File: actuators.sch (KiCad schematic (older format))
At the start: 16 parts

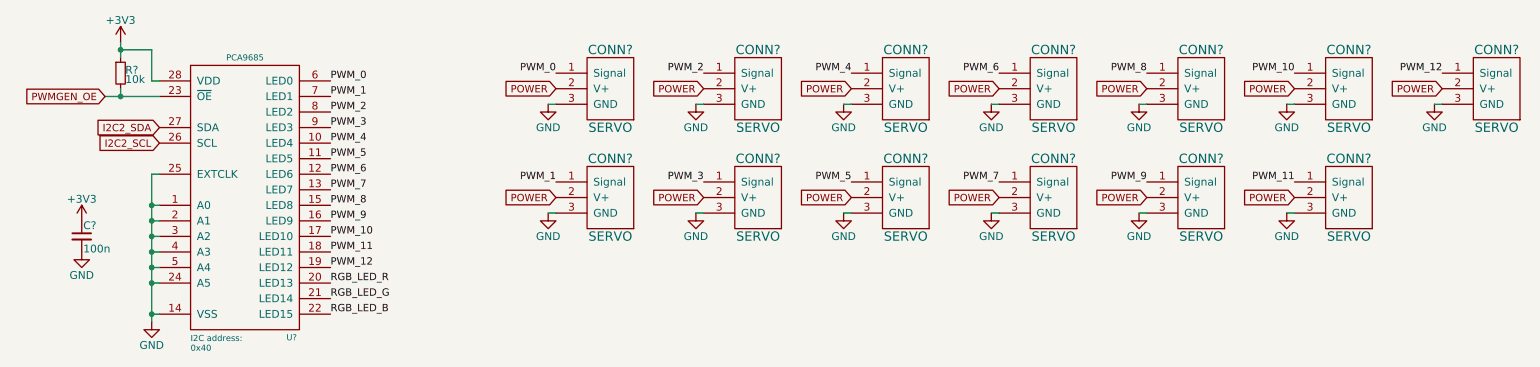
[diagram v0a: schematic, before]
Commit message: Add power from CAN bus and switch to hierarchical labelling
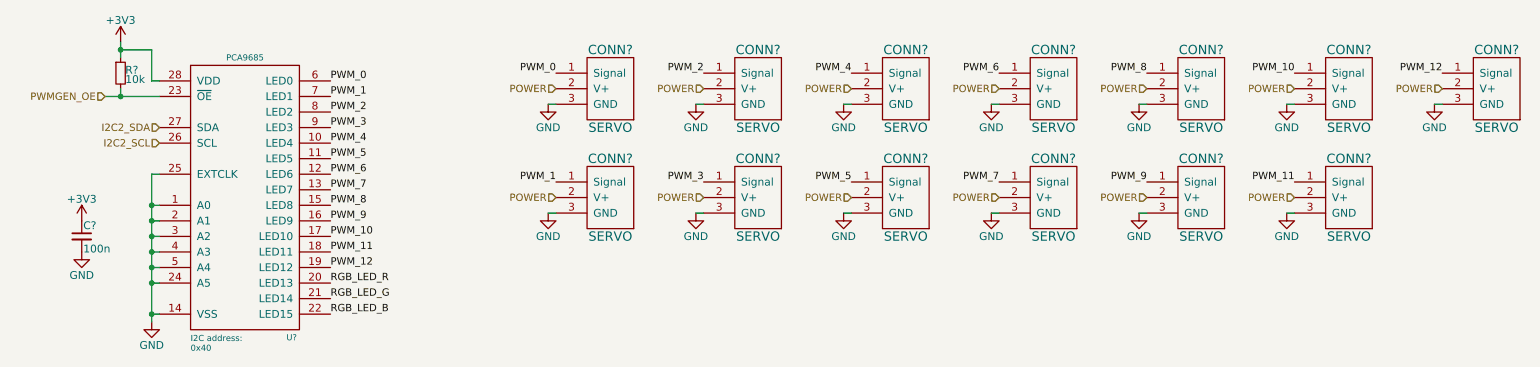
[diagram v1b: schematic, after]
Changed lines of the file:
@@
 Text Label 4300 1250 2    47   ~ 0
 PWM_0
-Text GLabel 4300 1350 0    47   Input ~ 0
-POWER
 $Comp
 L GND #PWR?
@@
 Text Label 5250 1250 2    47   ~ 0
 PWM_2
-Text GLabel 5250 1350 0    47   Input ~ 0
-POWER
 $Comp
 L GND #PWR?
@@
 Text Label 4300 1950 2    47   ~ 0
 PWM_1
-Text GLabel 4300 2050 0    47   Input ~ 0
-POWER
 $Comp
 L GND #PWR?
@@
 Text Label 5250 1950 2    47   ~ 0
 PWM_3
-Text GLabel 5250 2050 0    47   Input ~ 0
-POWER
 $Comp
 L GND #PWR?
@@
 Text Label 6200 1250 2    47   ~ 0
 PWM_4
-Text GLabel 6200 1350 0    47   Input ~ 0
-POWER
 $Comp
 L GND #PWR?
@@
 Text Label 7150 1250 2    47   ~ 0
 PWM_6
-Text GLabel 7150 1350 0    47   Input ~ 0
-POWER
 $Comp
 L GND #PWR?
@@
 Text Label 6200 1950 2    47   ~ 0
 PWM_5
-Text GLabel 6200 2050 0    47   Input ~ 0
-POWER
 $Comp
 L GND #PWR?
@@
 Text Label 7150 1950 2    47   ~ 0
 PWM_7
-Text GLabel 7150 2050 0    47   Input ~ 0
-POWER
 $Comp
 L GND #PWR?
@@
 Text Label 8100 1250 2    47   ~ 0
 PWM_8
-Text GLabel 8100 1350 0    47   Input ~ 0
-POWER
 $Comp
 L GND #PWR?
@@
 Text Label 9050 1250 2    47   ~ 0
 PWM_10
-Text GLabel 9050 1350 0    47   Input ~ 0
-POWER
 $Comp
 L GND #PWR?
@@
 Text Label 8100 1950 2    47   ~ 0
 PWM_9
-Text GLabel 8100 2050 0    47   Input ~ 0
-POWER
 $Comp
 L GND #PWR?
@@
 Text Label 9050 1950 2    47   ~ 0
 PWM_11
-Text GLabel 9050 2050 0    47   Input ~ 0
-POWER
 $Comp
 L GND #PWR?
@@
 Text Label 10000 1250 2    47   ~ 0
 PWM_12
-Text GLabel 10000 1350 0    47   Input ~ 0
-POWER
 $Comp
 L GND #PWR?
@@
 Wire Wire Line
 	9950 1450 10000 1450
-Text GLabel 1750 1600 0    47   Input ~ 0
+Text HLabel 1750 1600 0    47   Input ~ 0
 I2C2_SDA
-Text GLabel 1750 1700 0    47   Input ~ 0
+Text HLabel 1750 1700 0    47   Input ~ 0
 I2C2_SCL
-Text GLabel 1400 1400 0    47   Input ~ 0
+Text HLabel 1400 1400 0    47   Input ~ 0
 PWMGEN_OE
+Text HLabel 4300 1350 0    47   Input ~ 0
+POWER
+Text HLabel 4300 2050 0    47   Input ~ 0
+POWER
+Text HLabel 5250 1350 0    47   Input ~ 0
+POWER
+Text HLabel 5250 2050 0    47   Input ~ 0
+POWER
+Text HLabel 6200 2050 0    47   Input ~ 0
+POWER
+Text HLabel 6200 1350 0    47   Input ~ 0
+POWER
+Text HLabel 7150 1350 0    47   Input ~ 0
+POWER
+Text HLabel 7150 2050 0    47   Input ~ 0
+POWER
+Text HLabel 8100 2050 0    47   Input ~ 0
+POWER
+Text HLabel 8100 1350 0    47   Input ~ 0
+POWER
+Text HLabel 9050 1350 0    47   Input ~ 0
+POWER
+Text HLabel 9050 2050 0    47   Input ~ 0
+POWER
+Text HLabel 10000 1350 0    47   Input ~ 0
+POWER
 $EndSCHEMATC
